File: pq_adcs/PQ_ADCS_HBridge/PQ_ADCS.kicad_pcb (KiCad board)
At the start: 6 copper layers, 40 x 40 mm, 53 parts, among them J1 CES-110-02-L-S, J10 Pico-Clasp_01x09, J11 Pico-Clasp_01x15, J12 CES-102-02-L-S, J2 CES-110-02-L-S, J3 CES-110-02-L-S, J4 CES-110-02-L-S, J5 Pico-Clasp_01x03, J6 Pico-Clasp_01x10, J7 Pico-Clasp_01x10, J8 Pico-Clasp_01x10, J9 Pico-Clasp_01x10, U1 LPV542, U2 LPV542, U3 LPV542, U4 IIM-42652, U5 DRV8214RTER, U6 TMUX1108RSVR, U7 MMC5983MA, U8 DRV8214RTER, U9 DRV8214RTER

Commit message: update
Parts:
- moved R14 3.74 mm to (162.6, 107.6)
- moved R15 3.43 mm to (162.4, 104.0)
- moved U9 2.12 mm to (158.7, 103.2), turned to 180 degrees
- moved U8 1.36 mm to (159.4, 107.5), turned to -90 degrees
- moved R13 0.81 mm to (161.3, 99.4)
- moved U5 0.60 mm to (157.4, 99.0), turned to 180 degrees
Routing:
- net ADCS_POWER: track 1.65 -> 21.6 mm
- net Net-(U5-IPROPI): track 0.00 -> 3.24 mm
- net Net-(U8-IPROPI): track 0.00 -> 2.99 mm
- net Net-(U9-IPROPI): track 0.00 -> 2.66 mm
- net SOLAR_X: track 35.3 -> 36.5 mm
- net 3V3_PERM: track 58.4 -> 59.2 mm

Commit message: Restart
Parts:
- removed R13, R14, R15: 22k, Resistor_SMD:R_0603_1608Metric
- removed U8, U9: DRV8214RTER, DRV8214RTER:IC_DRV8214RTER
- added C11: 100 nF, Capacitor_SMD:C_0603_1608Metric, F.Cu at (159.4, 107.6)
- added C13: 1 uF, Capacitor_SMD:C_0603_1608Metric, F.Cu at (162.0, 103.9)
- added C14: 1 uF, Capacitor_SMD:C_0603_1608Metric, F.Cu at (159.4, 106.1)
- U5: value DRV8214RTER -> BD2606MVV; footprint DRV8214RTER:IC_DRV8214RTER -> Package_DFN_QFN:QFN-16-1EP_4x4mm_P0.65mm_EP2.5x2.5mm
- moved U5 3.79 mm to (158.0, 102.8), turned to 0 degrees
- renumbered U1 to U
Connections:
- C6 pad 2: /PHT5_ADCS -> /PHT6_ADCS
- J11 pad 2: /+MAG-Y -> /MAG-Y
- J11 pad 3: /-MAG-Y -> /VCC_MAG
- J12 pad 1: /-MAG+Y -> /VCC_MAG
- J12 pad 2: /+MAG+Y -> /MAG+Y
- J6 pad 2: /+MAG-X -> /MAG-X
- J6 pad 3: /-MAG-X -> /VCC_MAG
- J7 pad 2: /+MAG+X -> /MAG+X
- J7 pad 3: /-MAG+X -> /VCC_MAG
- J8 pad 2: /+MAG-Z -> /MAG-Z
- J8 pad 3: /-MAG-Z -> /VCC_MAG
- J9 pad 2: /+MAG+Z -> /MAG+Z
- J9 pad 3: /-MAG+Z -> /VCC_MAG
- R12 pad 1: /PHT5_ADCS -> /PHT6_ADCS
- U3 pad 7: /PHT5_ADCS -> /PHT6_ADCS
- U5 pad 1: Net-(U5-IPROPI) -> /MAG-X
- U5 pad 10: GND -> Net-(U5-C2P)
- U5 pad 11: ADCS_POWER -> GND
- U5 pad 12: GND -> /MAG+Y
- U5 pad 13: GND -> /MAG-Y
- U5 pad 14: SDA3 -> /MAG+Z
- U5 pad 15: SCL3 -> /MAG-Z
- U5 pad 16: 3V3_PERM -> /MAG+X
- U5 pad 2: 3V3_PERM -> SDA3
- U5 pad 3: GND -> SCL3
- U5 pad 4: GND -> ADCS_POWER
- U5 pad 5: 3V3_PERM -> /VCC_MAG
- U5 pad 6: /+MAG+X -> ADCS_POWER
- U5 pad 7: GND -> Net-(U5-C1N)
- U5 pad 8: /-MAG-X -> Net-(U5-C1P)
- U5 pad 9: GND -> Net-(U5-C2N)
- U6 pad 9: /PHT5_ADCS -> /PHT6_ADCS
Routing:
- net /VCC_MAG: track 0.00 -> 98.0 mm, vias 0 -> 7
- net (no net): track 63.4 -> 0.00 mm, vias 3 -> 0
- net /MAG+Z: track 0.00 -> 40.5 mm, vias 0 -> 2
- net /+MAG+Z: track 34.6 -> 0.00 mm, vias 2 -> 0
- net /MAG+Y: track 0.00 -> 26.7 mm, vias 0 -> 2
- net /MAG-Z: track 0.00 -> 23.3 mm, vias 0 -> 2
- net /MAG-X: track 0.00 -> 22.6 mm, vias 0 -> 2
- net /+MAG-X: track 21.8 -> 0.00 mm, vias 2 -> 0
- net /MAG-Y: track 0.00 -> 20.2 mm, vias 0 -> 2
- net /PHT6_ADCS: track 0.00 -> 19.8 mm
- net /PHT5_ADCS: track 33.6 -> 13.7 mm
- net /+MAG-Z: track 16.2 -> 0.00 mm, vias 2 -> 0
- net /+MAG-Y: track 13.7 -> 0.00 mm, vias 2 -> 0
- net /MAG+X: track 0.00 -> 8.50 mm, vias 0 -> 1
- net /+MAG+Y: track 6.37 -> 0.00 mm, vias 2 -> 0
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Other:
- board text added: "Mqt Actuators"

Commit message: Great advance
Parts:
- removed C11: 100 nF, Capacitor_SMD:C_0603_1608Metric
- removed C13, C14: 1 uF, Capacitor_SMD:C_0603_1608Metric
- added R13: 22k, Resistor_SMD:R_0603_1608Metric, F.Cu at (160.3, 95.6)
- added R14: 22k, Resistor_SMD:R_0603_1608Metric, F.Cu at (163.6, 98.5)
- added R15: 22k, Resistor_SMD:R_0603_1608Metric, F.Cu at (162.7, 106.9)
- added U8: DRV8214RTER, DRV8214RTER:IC_DRV8214RTER, F.Cu at (159.3, 99.5)
- added U9: DRV8214RTER, DRV8214RTER:IC_DRV8214RTER, F.Cu at (158.2, 105.4)
- U5: value BD2606MVV -> DRV8214RTER; footprint Package_DFN_QFN:QFN-16-1EP_4x4mm_P0.65mm_EP2.5x2.5mm -> DRV8214RTER:IC_DRV8214RTER
- moved U5 6.02 mm to (153.8, 98.4), turned to 180 degrees
- renumbered U to U1
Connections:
- J11 pad 2: /MAG-Y -> /+MAG-Y
- J11 pad 3: /VCC_MAG -> /-MAG-Y
- J12 pad 1: /VCC_MAG -> /+MAG-Y
- J12 pad 2: /MAG+Y -> /+MAG+Y
- J6 pad 2: /MAG-X -> /+MAG-X
- J6 pad 3: /VCC_MAG -> /-MAG-X
- J7 pad 2: /MAG+X -> /+MAG+X
- J7 pad 3: /VCC_MAG -> /+MAG-X
- J8 pad 2: /MAG-Z -> /+MAG-Z
- J8 pad 3: /VCC_MAG -> /-MAG-Z
- J9 pad 2: /MAG+Z -> /+MAG+Z
- J9 pad 3: /VCC_MAG -> /+MAG-Z
- U5 pad 1: /MAG-X -> Net-(U5-IPROPI)
- U5 pad 10: Net-(U5-C2P) -> GND
- U5 pad 11: GND -> ADCS_POWER
- U5 pad 12: /MAG+Y -> GND
- U5 pad 13: /MAG-Y -> GND
- U5 pad 14: /MAG+Z -> SDA3
- U5 pad 15: /MAG-Z -> SCL3
- U5 pad 16: /MAG+X -> 3V3_PERM
- U5 pad 2: SDA3 -> 3V3_PERM
- U5 pad 3: SCL3 -> GND
- U5 pad 4: ADCS_POWER -> GND
- U5 pad 5: /VCC_MAG -> 3V3_PERM
- U5 pad 6: ADCS_POWER -> /+MAG+X
- U5 pad 7: Net-(U5-C1N) -> GND
- U5 pad 8: Net-(U5-C1P) -> /-MAG-X
- U5 pad 9: Net-(U5-C2N) -> GND
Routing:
- net /VCC_MAG: track 98.0 -> 0.00 mm, vias 7 -> 0
- net /+MAG+Z: track 0.00 -> 57.8 mm, vias 0 -> 4
- net /MAG+Z: track 40.5 -> 0.00 mm, vias 2 -> 0
- net /+MAG-X: track 0.00 -> 38.3 mm, vias 0 -> 2
- net 3V3_PERM: track 58.4 -> 91.4 mm, vias 12 -> 18
- net /-MAG-Z: track 0.00 -> 29.4 mm, vias 0 -> 4
- net /+MAG-Z: track 0.00 -> 27.9 mm, vias 0 -> 2
- net /MAG+Y: track 26.7 -> 0.00 mm, vias 2 -> 0
- net /MAG-Z: track 23.3 -> 0.00 mm, vias 2 -> 0
- net /MAG-X: track 22.6 -> 0.00 mm, vias 2 -> 0
- net /+MAG+Y: track 0.00 -> 21.3 mm, vias 0 -> 2
- net SDA3: track 129.8 -> 151.1 mm, vias 8 -> 9
- net /-MAG-X: track 0.00 -> 20.4 mm, vias 0 -> 2
- net /MAG-Y: track 20.2 -> 0.00 mm, vias 2 -> 0
- net /-MAG-Y: track 0.00 -> 18.1 mm, vias 0 -> 2
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
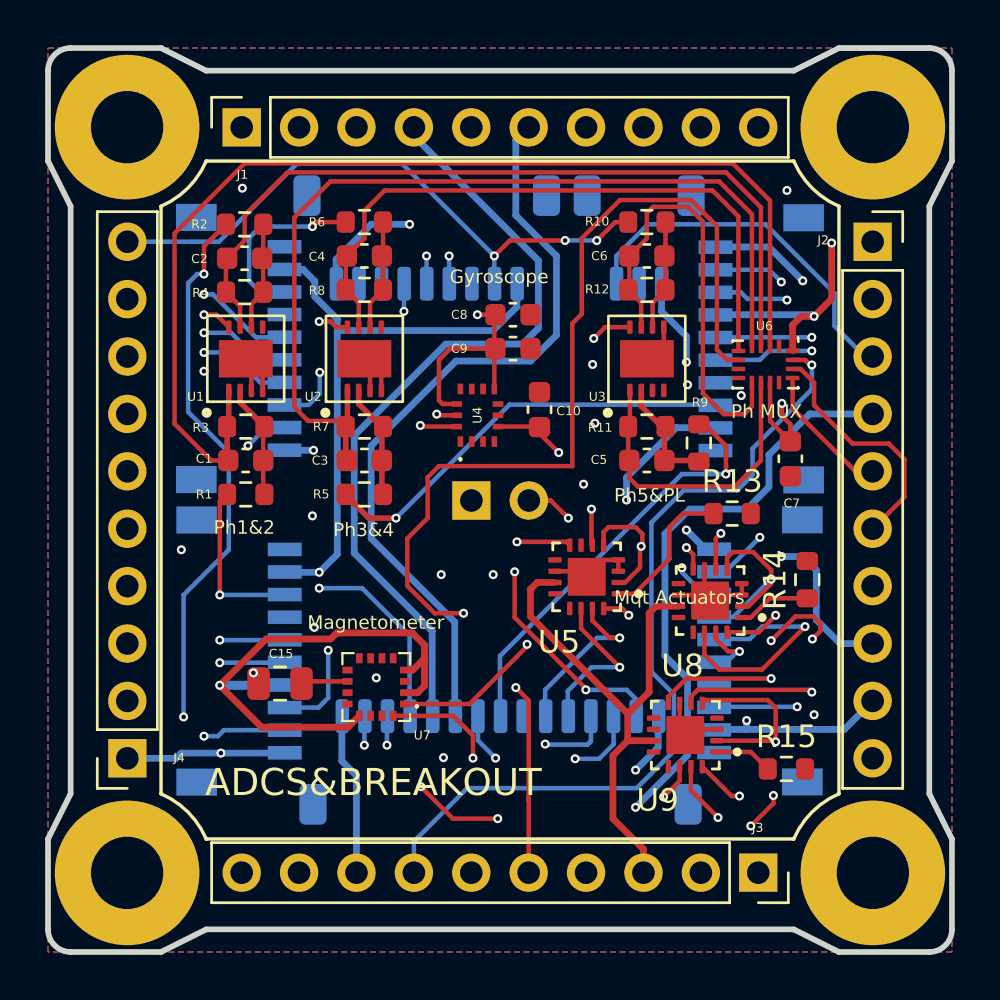
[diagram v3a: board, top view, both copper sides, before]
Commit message: No errors, but still warnings
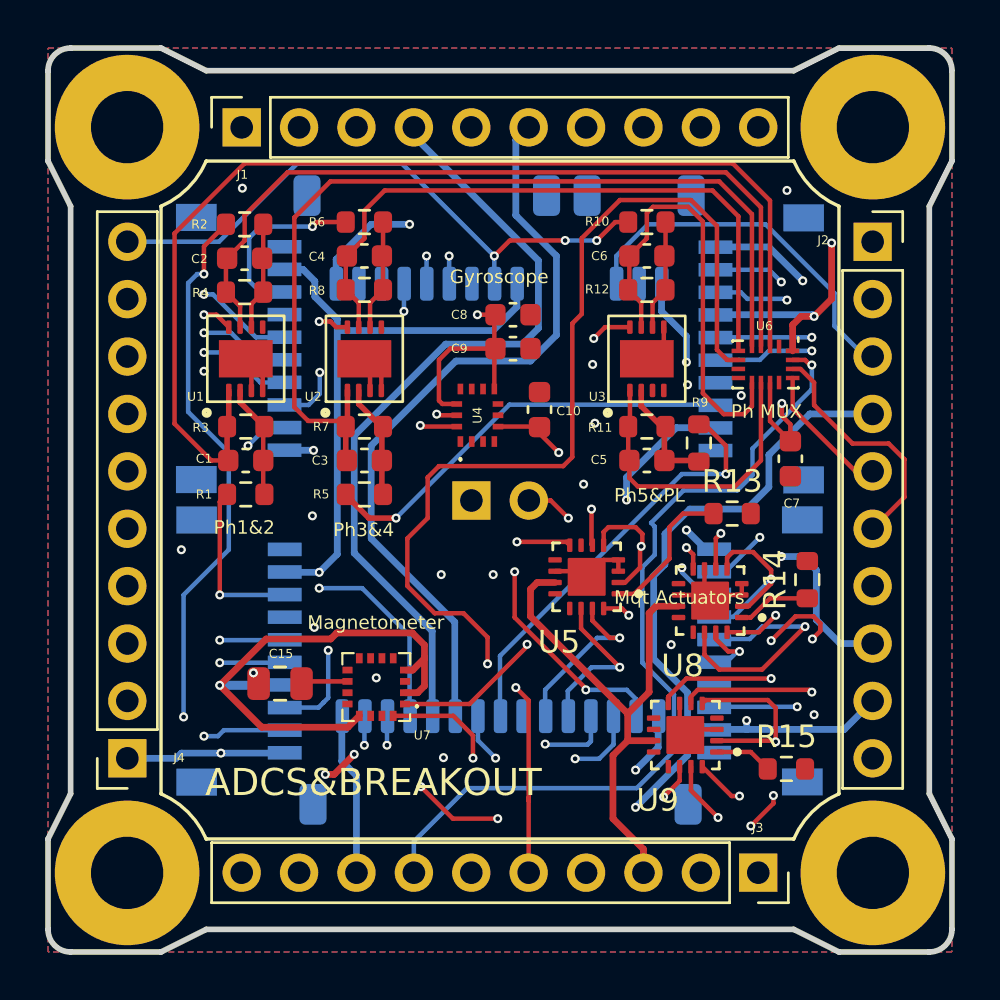
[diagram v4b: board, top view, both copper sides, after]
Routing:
- net SOLAR_X: track 36.3 -> 38.1 mm, vias 2 -> 4
- net GND: vias 17 -> 18
